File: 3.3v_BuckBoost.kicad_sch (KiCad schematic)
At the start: 4 parts, among them U801 TPS63031DSK

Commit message: "PCB front Layer Component assembly done"
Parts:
- added TP801: 3.3V, TestPoint:TestPoint_Pad_D1.0mm, symbol Connector:TestPoint
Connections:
- net +3V3: now also TP801.1

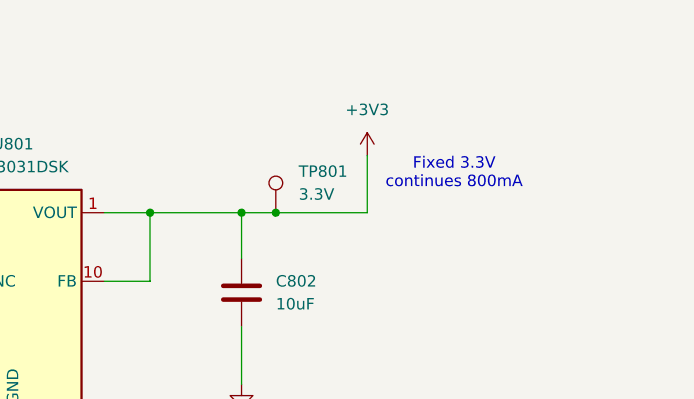
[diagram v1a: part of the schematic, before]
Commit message: "Before changing the orientation of the LoRa module. removing existing LoRa module routing."
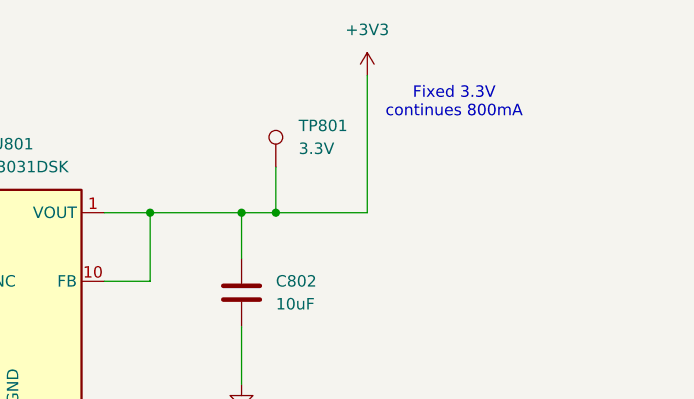
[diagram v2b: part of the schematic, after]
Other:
- moved on the sheet: TP801
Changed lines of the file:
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@@
 	(text "Fixed 3.3V \ncontinues 800mA"
 		(exclude_from_sim no)
-		(at 192.532 79.502 0)
+		(at 192.532 71.628 0)
 		(effects
 			(font
@@
 	(wire
 		(pts
-			(xy 182.88 77.47) (xy 182.88 83.82)
+			(xy 182.88 68.58) (xy 182.88 83.82)
 		)
 		(stroke
@@
 		(pts
 			(xy 106.68 83.82) (xy 114.3 83.82)
+		)
+		(stroke
+			(width 0)
+			(type default)
+		)
+	)
+	(wire
+		(pts
+			(xy 172.72 78.74) (xy 172.72 83.82)
 		)
 		(stroke
@@
 	(symbol
 		(lib_id "power:+3V3")
-		(at 182.88 77.47 0)
+		(at 182.88 68.58 0)
 		(unit 1)
 		(exclude_from_sim no)
@@
 		(fields_autoplaced yes)
 		(property "Reference" "#PWR0804"
-			(at 182.88 81.28 0)
+			(at 182.88 72.39 0)
 			(effects
 				(font
@@
 		)
 		(property "Value" "+3V3"
-			(at 182.88 72.39 0)
+			(at 182.88 63.5 0)
 			(effects
 				(font
@@
 		)
 		(property "Footprint" ""
-			(at 182.88 77.47 0)
+			(at 182.88 68.58 0)
 			(effects
 				(font
@@
 		)
 		(property "Datasheet" ""
-			(at 182.88 77.47 0)
+			(at 182.88 68.58 0)
 			(effects
 				(font
@@
 		)
 		(property "Description" "Power symbol creates a global label with name \"+3V3\""
-			(at 182.88 77.47 0)
+			(at 182.88 68.58 0)
 			(effects
 				(font
@@
 	(symbol
 		(lib_id "Connector:TestPoint")
-		(at 172.72 83.82 0)
+		(at 172.72 78.74 0)
 		(unit 1)
 		(exclude_from_sim no)
@@
 		(fields_autoplaced yes)
 		(property "Reference" "TP801"
-			(at 175.26 79.2479 0)
+			(at 175.26 74.1679 0)
 			(effects
 				(font
@@
 		)
 		(property "Value" "3.3V"
-			(at 175.26 81.7879 0)
+			(at 175.26 76.7079 0)
 			(effects
 				(font
@@
 		)
 		(property "Footprint" "TestPoint:TestPoint_Pad_D1.0mm"
-			(at 177.8 83.82 0)
+			(at 177.8 78.74 0)
 			(effects
 				(font
@@
 		)
 		(property "Datasheet" "~"
-			(at 177.8 83.82 0)
+			(at 177.8 78.74 0)
 			(effects
 				(font
@@
 		)
 		(property "Description" "test point"
-			(at 172.72 83.82 0)
-			(effects
-				(font
+			(at 172.72 78.74 0)
+			(effects
+				(font
